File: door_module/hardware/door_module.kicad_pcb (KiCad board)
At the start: 2 copper layers, 178 parts, among them J1 Raspberry Pi, J10 Screw_Terminal_01x02, J14 , J15 , J17 , J18 , J2 Conn_02x02_Odd_Even, J20 Screw_Terminal_01x02, J3 Cat7 from Server, J30 Screw_Terminal_01x02, J40 Screw_Terminal_01x02, J50 Screw_Terminal_01x06, J6 , J60 Screw_Terminal_01x04, J61 FT4232_1, J7 , J70 Screw_Terminal_01x04, J71 FT4232_1, J8 , J80 Screw_Terminal_01x04, J81 FT4232_1, J9 , J90 Screw_Terminal_01x04, J91 FT4232_1, Q11 IRF7404, Q2 IRF6614, Q66 BC557, Q76 BC557, Q86 BC557, Q96 BC557, U1 TMA 1205S, U10 LTV-817, U1001 LTV-817, U2 LP2950-5.0_TO92, U21 LTV-817, U3 LP2950-3.3_TO92, U31 LTV-817, U41 LTV-817, U51 LTV-817, U52 LTV-817, U53 LTV-817, U54 LTV-817, U61 LTV-817, U62 LTV-817, U71 LTV-817, U72 LTV-817, U81 LTV-817, U82 LTV-817, U91 LTV-817

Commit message: Some more Groups on the door_module PCB
Signed-off-by: Juergen G. Schimmer <schimmi2@gmail.com>
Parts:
- moved J1 268.1 mm to (76.2, 138.4)
- moved TP_5V1 222.0 mm to (86.4, 43.2)
- moved J70 201.0 mm to (276.9, 127.0), turned to 90 degrees
- moved J90 193.4 mm to (276.9, 76.2), turned to 90 degrees
- moved R77 192.9 mm to (271.8, 124.5), turned to 90 degrees
- moved R76 189.8 mm to (269.2, 124.5), turned to 180 degrees
- moved R97 185.6 mm to (271.8, 73.7), turned to 90 degrees
- moved D77 183.9 mm to (269.2, 108.0), turned to 180 degrees
- moved D76 182.1 mm to (269.2, 114.3), turned to 180 degrees
- moved R96 181.4 mm to (269.2, 73.7), turned to 180 degrees
- moved D97 180.7 mm to (269.2, 57.1), turned to 180 degrees
- moved R78 178.7 mm to (261.6, 110.5)
- moved J15 176.8 mm to (61.0, 106.7)
- moved Q76 175.3 mm to (268.0, 120.7), turned to 90 degrees
- moved D96 175.3 mm to (269.2, 63.5), turned to 180 degrees
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
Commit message: First alpha PCB
Signed-off-by: Juergen G. Schimmer <schimmi2@gmail.com>
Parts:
- removed D10: ZPD24, Diode_THT:D_DO-35_SOD27_P10.16mm_Horizontal
- removed D2, D3, D4, D5, D6, D7, D8: 1N4007, Diode_THT:D_DO-41_SOD81_P10.16mm_Horizontal
- removed D9: LED, LED_THT:LED_D5.0mm
- removed J30, J40: Screw_Terminal_01x02, Connector_Phoenix_MSTB:PhoenixContact_MSTBA_2,5_2-G-5,08_1x02_P5.08mm_Horizontal
- removed Q2: IRF6614, Package_DirectFET:DirectFET_ST
- removed R1: 25k, Resistor_THT:R_Axial_DIN0207_L6.3mm_D2.5mm_P10.16mm_Horizontal
- removed R2: 2k2, Resistor_THT:R_Axial_DIN0207_L6.3mm_D2.5mm_P10.16mm_Horizontal
- removed R3: 2R2, Resistor_THT:R_Axial_DIN0207_L6.3mm_D2.5mm_P10.16mm_Horizontal
- removed R4: 10k, Resistor_THT:R_Axial_DIN0207_L6.3mm_D2.5mm_P10.16mm_Horizontal
- removed TP_+48POE1, TP_-48POE1, TP_GND2: TestPoint, TestPoint:TestPoint_Loop_D2.60mm_Drill1.6mm_Beaded
- added J21: Conn_01x01_Male, Connector_PinHeader_2.54mm:PinHeader_1x01_P2.54mm_Vertical, F.Cu at (74.9, 61.0)
- added J22: Conn_01x01_Male, Connector_PinHeader_2.54mm:PinHeader_1x01_P2.54mm_Vertical, F.Cu at (72.4, 61.0)
- added J23: Conn_01x01_Male, Connector_PinHeader_2.54mm:PinHeader_1x01_P2.54mm_Vertical, F.Cu at (77.5, 61.0)
- added J24: Conn_01x01_Male, Connector_PinHeader_2.54mm:PinHeader_1x01_P2.54mm_Vertical, F.Cu at (69.8, 61.0)
- added J26: Conn_01x01_Male, Connector_PinHeader_2.54mm:PinHeader_1x01_P2.54mm_Vertical, F.Cu at (94.0, 61.0)
- added J27: Conn_01x01_Male, Connector_PinHeader_2.54mm:PinHeader_1x01_P2.54mm_Vertical, F.Cu at (90.8, 61.0)
- added J28: Conn_01x01_Male, Connector_PinHeader_2.54mm:PinHeader_1x01_P2.54mm_Vertical, F.Cu at (97.2, 61.0)
- added J31: Screw_Terminal_01x02, Connector_Phoenix_MSTB:PhoenixContact_MSTBA_2,5_2-G-5,08_1x02_P5.08mm_Horizontal, F.Cu at (36.8, 57.8)
- added J32: Screw_Terminal_01x02, Connector_Phoenix_MSTB:PhoenixContact_MSTBA_2,5_2-G-5,08_1x02_P5.08mm_Horizontal, F.Cu at (36.8, 84.5)
- added J41: Screw_Terminal_01x02, Connector_Phoenix_MSTB:PhoenixContact_MSTBA_2,5_2-G-5,08_1x02_P5.08mm_Horizontal, F.Cu at (36.8, 97.8)
- added J42: Screw_Terminal_01x02, Connector_Phoenix_MSTB:PhoenixContact_MSTBA_2,5_2-G-5,08_1x02_P5.08mm_Horizontal, F.Cu at (36.8, 111.1)
- added R32: 470, Resistor_THT:R_Axial_DIN0207_L6.3mm_D2.5mm_P10.16mm_Horizontal, F.Cu at (50.8, 90.8)
- added R37: 3k3, Resistor_THT:R_Axial_DIN0207_L6.3mm_D2.5mm_P10.16mm_Horizontal, F.Cu at (73.7, 90.8)
- added R42: 470, Resistor_THT:R_Axial_DIN0207_L6.3mm_D2.5mm_P10.16mm_Horizontal, F.Cu at (50.8, 111.8)
- added R47: 3k3, Resistor_THT:R_Axial_DIN0207_L6.3mm_D2.5mm_P10.16mm_Horizontal, F.Cu at (73.7, 111.8)
- added U32: LTV-817, Package_DIP:DIP-4_W7.62mm, F.Cu at (53.3, 88.3)
- added U42: LTV-817, Package_DIP:DIP-4_W7.62mm, F.Cu at (53.3, 109.2)
- J61, J71, J81, J91: footprint Connector_PinSocket_2.54mm:PinSocket_1x11_P2.54mm_Vertical -> Connector_PinSocket_2.54mm:PinSocket_1x12_P2.54mm_Vertical
- JP61, JP62, JP71, JP72, JP81, JP82, JP91, JP92: moved to B.Cu
- Q11: footprint Package_SO:SOIC-8_3.9x4.9mm_P1.27mm -> Package_TO_SOT_THT:TO-220-3_Vertical
- R41: value 3k3 -> 470
- R46: value 470 -> 3k3
- TP61, TP62, TP63, TP64, TP65, TP66, TP67, TP68, TP69, TP71, TP72, TP73, TP74, TP75, TP76, TP77, TP78, TP79, TP81, TP82, TP83, TP84, TP85, TP86, TP87, TP88, TP89, TP91, TP92, TP93, TP94, TP95, TP96, TP97, TP98, TP99: footprint TestPoint:TestPoint_Loop_D2.60mm_Drill1.6mm_Beaded -> TestPoint:TestPoint_Loop_D1.80mm_Drill1.0mm_Beaded
- U1: footprint Package_SIP:PowerIntegrations_eSIP-7F -> Package_SIP:SIP9_Housing_BigPads
- moved J3 174.3 mm to (107.3, 134.0), turned to 270 degrees
- moved C6 171.9 mm to (174.6, 151.9), turned to 90 degrees
- moved J7 170.3 mm to (114.3, 136.5)
- moved J6 169.7 mm to (114.3, 133.3)
- moved J9 168.5 mm to (114.3, 139.7)
- moved C7 162.2 mm to (159.4, 149.2), turned to 90 degrees
- moved TP_3V3A1 161.9 mm to (159.4, 143.5), turned to 270 degrees
- moved J8 161.7 mm to (114.3, 130.2)
- moved U3 160.8 mm to (155.6, 146.7), turned to 270 degrees
- moved C8 150.3 mm to (148.0, 145.5), turned to 270 degrees
- moved C9 149.6 mm to (152.4, 145.5), turned to 270 degrees
- moved D1 121.9 mm to (92.1, 116.2), turned to 270 degrees
- moved U2 114.3 mm to (183.5, 57.1), turned to 180 degrees
- moved C4 114.0 mm to (178.4, 57.1), turned to 270 degrees
- moved C3 114.0 mm to (164.5, 50.8), turned to 270 degrees
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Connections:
- D1 pad 1: Net-(D1-Pad1) -> +12V
- D1 pad 2: Net-(D1-Pad2) -> /bl
- J1 pad 11: BELL_LED_R -> BELL_BUTTON
- J1 pad 12: DOOR_CLOSER -> /GPIO1
- J1 pad 13: BELL_LED_G -> Sabotage2
- J1 pad 15: BELL_LED_B -> Sabotage1
- J1 pad 16: FB_STRIKE -> /GPIO4
- J1 pad 18: FB_MAGNET -> /GPIO5
- J1 pad 21: Net-(J1-Pad21) -> FB_MAGNET
- J1 pad 22: STRIKE -> /GPIO6
- J1 pad 23: Net-(J1-Pad23) -> FB_STRIKE
- J1 pad 3: Net-(J1-Pad3) -> BELL_LED_B
- J1 pad 33: Net-(J1-Pad33) -> DOOR_CLOSER
- J1 pad 37: Net-(J1-Pad37) -> STRIKE
- J1 pad 5: Net-(J1-Pad5) -> BELL_LED_G
- J1 pad 7: BELL_BUTTON -> BELL_LED_R
- J2 pad 1: Net-(D1-Pad2) -> Net-(J2-Pad1)
- J3 pad 4: +12V -> /bl
- J3 pad 5: +12V -> /bl
- Q11 pad 1: Net-(C11-Pad1) -> Net-(D11-Pad1)
- Q11 pad 2: Net-(C11-Pad1) -> Net-(D12-Pad2)
- R41 pad 1: GND -> Net-(R41-Pad1)
- R41 pad 2: FB_MAGNET -> Net-(J41-Pad1)
- R46 pad 1: Net-(R46-Pad1) -> GND
- R46 pad 2: Net-(J40-Pad1) -> Sabotage1
- U41 pad 2: Net-(R46-Pad1) -> Net-(R41-Pad1)
- U41 pad 3: FB_MAGNET -> Sabotage1
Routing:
- net GNDA: track 0.00 -> 558.8 mm
- net GND: track 0.00 -> 540.8 mm
- net +5VA: track 0.00 -> 357.5 mm
- net +12VA: track 0.00 -> 108.0 mm
- net +3.3VP: track 0.00 -> 107.1 mm
- net +3.3VA: track 0.00 -> 105.6 mm
- net +5V: track 0.00 -> 100.8 mm
- net +12V: track 0.00 -> 93.8 mm
- net +3V3: track 0.00 -> 73.6 mm
- net Net-(C11-Pad1): track 0.00 -> 66.4 mm
- net RX_USB0: track 0.00 -> 49.8 mm
- net RX_USB3: track 0.00 -> 44.9 mm
- net TX_USB0: track 0.00 -> 43.5 mm
- net BELL_BUTTON: track 0.00 -> 40.7 mm
- net RX_USB1: track 0.00 -> 36.1 mm
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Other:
- board outline added: 162.6 x 113 mm
- net class 50mil added: clearance 0.2, trace_width 1.23, via_dia 1.23, via_drill 0.6
- net class Breit added: clearance 0.2, trace_width 2, via_dia 2, via_drill 1

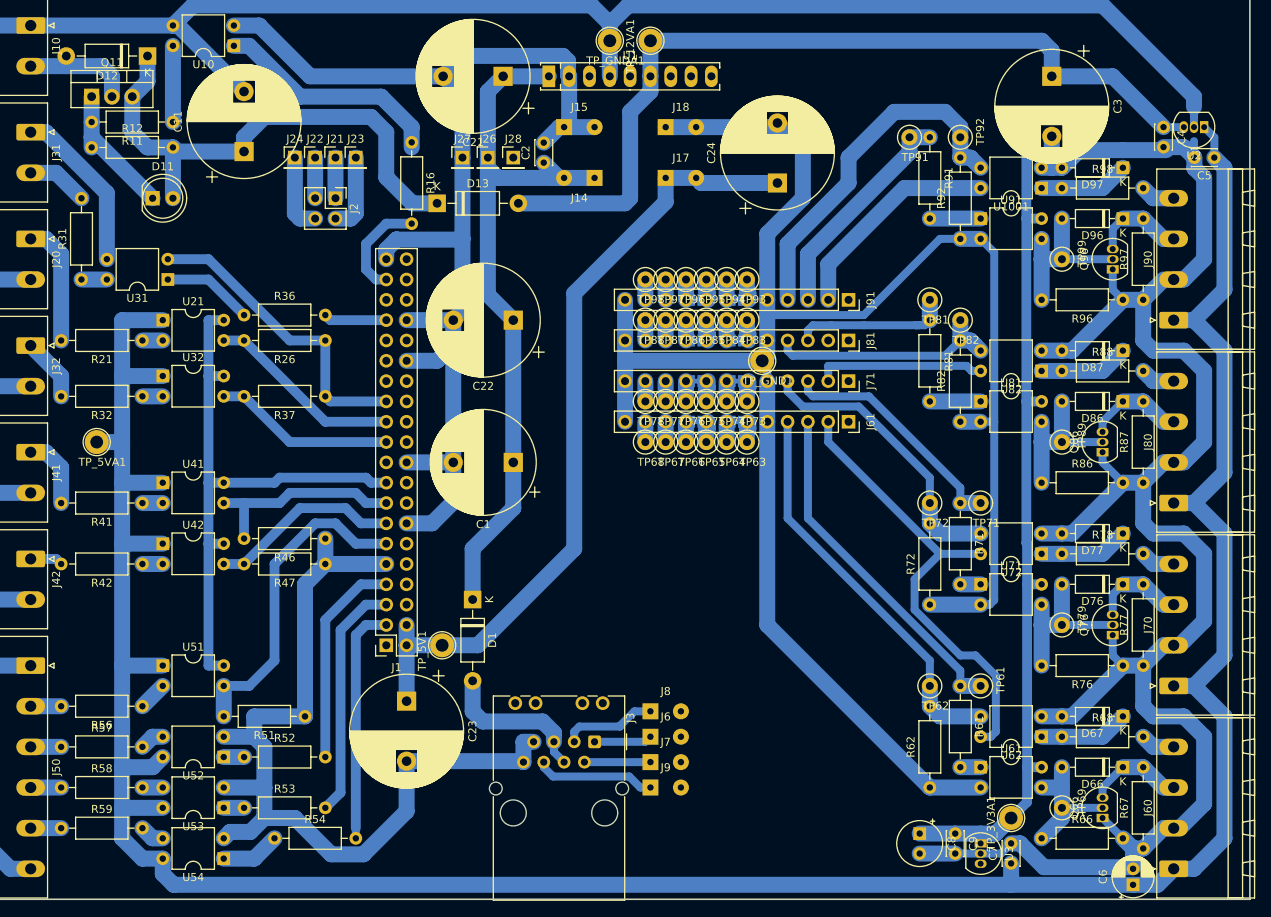
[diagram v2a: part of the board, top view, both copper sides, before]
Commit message: -mod: Changed U2 VoltegeRegulatior to LM7805CT
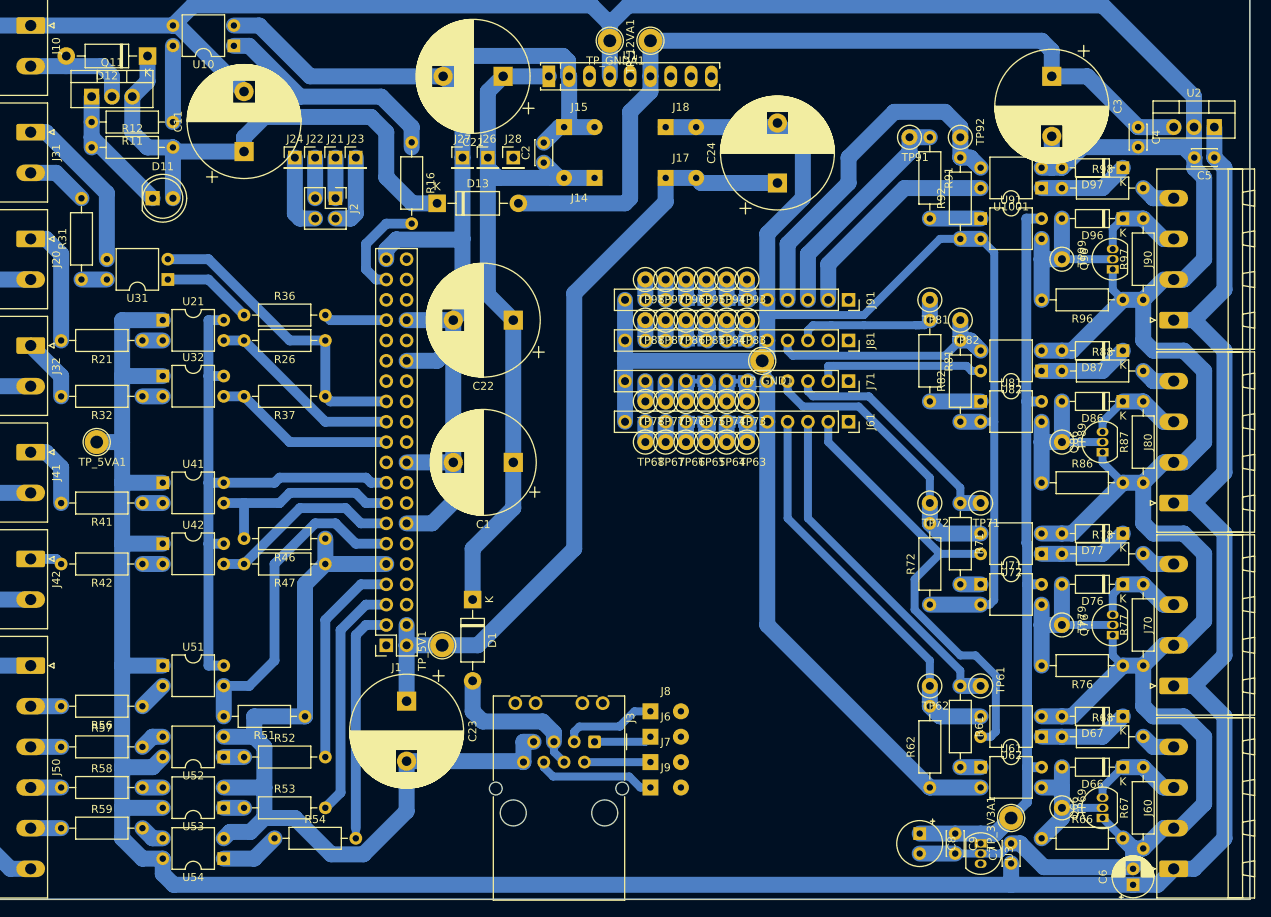
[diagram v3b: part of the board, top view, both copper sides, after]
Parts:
- U2: value LP2950-5.0_TO92 -> LM7805CT; footprint Package_TO_SOT_THT:TO-92_Inline -> Package_TO_SOT_THT:TO-220-3_Vertical
- moved U2 3.81 mm to (179.7, 57.1), turned to 0 degrees
- moved C4 3.18 mm to (175.3, 57.1)
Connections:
- J1 pad 10: Net-(J1-Pad10) -> unconnected-(J1-Pad10)
- J1 pad 19: Net-(J1-Pad19) -> unconnected-(J1-Pad19)
- J1 pad 24: Net-(J1-Pad24) -> unconnected-(J1-Pad24)
- J1 pad 26: Net-(J1-Pad26) -> unconnected-(J1-Pad26)
- J1 pad 27: Net-(J1-Pad27) -> unconnected-(J1-Pad27)
- J1 pad 28: Net-(J1-Pad28) -> unconnected-(J1-Pad28)
- J1 pad 29: Net-(J1-Pad29) -> unconnected-(J1-Pad29)
- J1 pad 31: Net-(J1-Pad31) -> unconnected-(J1-Pad31)
- J1 pad 32: Net-(J1-Pad32) -> unconnected-(J1-Pad32)
- J1 pad 35: Net-(J1-Pad35) -> unconnected-(J1-Pad35)
- J1 pad 36: Net-(J1-Pad36) -> unconnected-(J1-Pad36)
- J1 pad 38: Net-(J1-Pad38) -> unconnected-(J1-Pad38)
- J1 pad 40: Net-(J1-Pad40) -> unconnected-(J1-Pad40)
- J1 pad 8: Net-(J1-Pad8) -> unconnected-(J1-Pad8)
- J28 pad 1: Net-(J28-Pad1) -> unconnected-(J28-Pad1)
- U1 pad 5: Net-(U1-Pad5) -> unconnected-(U1-Pad5)
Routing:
- net +3.3VA: track 105.6 -> 96.7 mm
- net Net-(J91-Pad9): track 2.54 -> 5.15 mm
- net Net-(J91-Pad8): track 2.61 -> 0.00 mm
- net Net-(J81-Pad9): track 2.54 -> 5.15 mm
- net Net-(J81-Pad8): track 2.61 -> 0.00 mm
- net Net-(J71-Pad9): track 2.54 -> 5.15 mm
- net Net-(J71-Pad8): track 2.61 -> 0.00 mm
- net Net-(J91-Pad7): track 2.54 -> 0.00 mm
- net Net-(J91-Pad6): track 2.61 -> 5.15 mm
- net Net-(J81-Pad7): track 2.54 -> 0.00 mm
- net Net-(J81-Pad6): track 2.61 -> 5.15 mm
- net Net-(J71-Pad7): track 2.54 -> 0.00 mm
- net Net-(J71-Pad6): track 2.61 -> 5.15 mm
- net Net-(J61-Pad9): track 2.54 -> 0.00 mm
- net Net-(J61-Pad8): track 2.61 -> 5.15 mm
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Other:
- net class 50mil removed
- net class Breit removed
- net class Default removed
